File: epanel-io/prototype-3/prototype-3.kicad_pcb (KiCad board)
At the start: 2 copper layers, 87 x 68 mm, 32 parts, among them J1 Conn_01x07_Male, J2 Screw_Terminal_01x04, J3 Screw_Terminal_01x04, J4 Screw_Terminal_01x02, Q1 IRF830, Q2 IRF830, Q3 IRF830, U2 4N35, U3 4N35, U4 H11AA1, U5 H11AA1, U6 H11AA1

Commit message: wip proto 3
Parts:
- removed J4: Screw_Terminal_01x02, TerminalBlock:TerminalBlock_bornier-2_P5.08mm
- added C2: 2.2uF/63V, Capacitor_SMD:C_1206_3216Metric, F.Cu at (144.8, 69.8)
- added D4: 1N4007, Diode_SMD:D_SMA, F.Cu at (139.7, 67.3)
- added JP1: Jumper_2_Bridged, Connector_PinHeader_2.54mm:PinHeader_1x02_P2.54mm_Vertical, F.Cu at (95.2, 110.5)
- added Q4: IRF830, Package_TO_SOT_SMD:TO-263-3_TabPin2, F.Cu at (174.4, 73.7)
- added R16: 33KΩ/0.5W, Resistor_SMD:R_0805_2012Metric, F.Cu at (141.0, 61.0)
- added R17: 33KΩ/0.5W, Resistor_SMD:R_0805_2012Metric, F.Cu at (141.0, 72.4)
- added U1: Pico, MCU_RaspberryPi_and_Boards:RPi_Pico_SMD_TH, F.Cu at (149.9, 152.4)
- D1: value 4* 1N5408 -> 10V/0.4W; footprint Diode_SMD:Diode_Bridge_Diotec_SO-DIL-Slim -> Diode_SMD:D_SOD-123
- J1: value Conn_01x07_Male -> Conn_01x05_Male; footprint Connector_PinHeader_2.54mm:PinHeader_1x07_P2.54mm_Vertical -> Connector_PinHeader_2.54mm:PinHeader_1x05_P2.54mm_Vertical
- J2, J3: value Screw_Terminal_01x04 -> Screw_Terminal_01x03; footprint TerminalBlock:TerminalBlock_bornier-4_P5.08mm -> TerminalBlock:TerminalBlock_bornier-3_P5.08mm
- PS1: value HLK-PM12 -> HLK-PM01
- moved R3 109.8 mm to (215.5, 149.8)
- moved R5 105.9 mm to (215.5, 147.3)
- moved R4 98.3 mm to (212.1, 129.5)
- moved J3 86.9 mm to (111.8, 55.9), turned to -90 degrees
- moved R12 83.8 mm to (119.4, 55.9), turned to -90 degrees
- moved R13 76.2 mm to (119.4, 62.2), turned to -90 degrees
- moved U4 74.5 mm to (146.1, 127.0), turned to -90 degrees
- moved R1 58.5 mm to (168.9, 125.7), turned to 0 degrees
- moved R2 54.8 mm to (168.1, 123.2), turned to 0 degrees
- moved PS1 52.1 mm to (139.7, 17.8), turned to -90 degrees
- moved R14 50.2 mm to (124.5, 55.9), turned to -90 degrees
- moved D3 47.7 mm to (139.7, 55.9), turned to 90 degrees
- moved R15 47.6 mm to (124.5, 62.2), turned to -90 degrees
- moved U5 45.6 mm to (137.2, 127.0), turned to -90 degrees
- moved R10 45.2 mm to (121.9, 55.9), turned to -90 degrees
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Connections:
- D1 pad 1: Net-(D1-Pad1) -> Net-(C1-Pad1)
- D1 pad 2: Net-(D1-Pad2) -> Net-(C1-Pad2)
- D2 pad 1: Net-(C1-Pad1) -> Net-(C2-Pad1)
- D2 pad 2: Net-(C1-Pad2) -> Net-(C2-Pad2)
- D3 pad 2: Net-(D3-Pad2) -> NEUT
- J1 pad 1: +3V3 -> +5V
- J2 pad 1: Net-(D1-Pad3) -> LINE
- J2 pad 2: Net-(D1-Pad4) -> Net-(J2-Pad2)
- J3 pad 1: Net-(D3-Pad2) -> NEUT
- PS1 pad 1: Net-(D1-Pad3) -> LINE
- PS1 pad 2: Net-(J2-Pad4) -> NEUT
- PS1 pad 3: Net-(D1-Pad2) -> GND
- PS1 pad 4: Net-(PS1-Pad4) -> +5V
- Q1 pad 2: Net-(D1-Pad1) -> LINE
- Q1 pad 3: Net-(D1-Pad2) -> Net-(C1-Pad2)
- Q2 pad 1: Net-(Q2-Pad1) -> Net-(Q1-Pad1)
- Q2 pad 2: Net-(D3-Pad2) -> Net-(J2-Pad2)
- Q3 pad 1: Net-(Q2-Pad1) -> Net-(Q3-Pad1)
- Q3 pad 2: Net-(J3-Pad2) -> LINE
- Q3 pad 3: Net-(C1-Pad2) -> Net-(C2-Pad2)
- R1 pad 2: Net-(J1-Pad3) -> Net-(R1-Pad2)
- R10 pad 1: Net-(J3-Pad4) -> NEUT
- R11 pad 1: Net-(J3-Pad3) -> Net-(J3-Pad2)
- R12 pad 1: Net-(J4-Pad1) -> NEUT
- R12 pad 2: Net-(R12-Pad2) -> Net-(U5-Pad1)
- R13 pad 1: Net-(J4-Pad2) -> Net-(J3-Pad3)
- R14 pad 1: Net-(R14-Pad1) -> NEUT
- R14 pad 2: Net-(C1-Pad1) -> Net-(R14-Pad2)
- R15 pad 1: Net-(D3-Pad1) -> LINE
- R15 pad 2: Net-(R14-Pad1) -> Net-(R15-Pad2)
- R2 pad 2: Net-(J1-Pad5) -> Net-(R2-Pad2)
- R3 pad 1: Net-(J1-Pad4) -> Net-(R3-Pad1)
- R4 pad 1: Net-(J1-Pad6) -> Net-(R4-Pad1)
- R5 pad 1: Net-(J1-Pad7) -> Net-(R5-Pad1)
- R6 pad 2: Net-(D1-Pad2) -> Net-(C1-Pad2)
- R7 pad 1: Net-(Q2-Pad1) -> Net-(Q3-Pad1)
- R7 pad 2: Net-(C1-Pad2) -> Net-(C2-Pad2)
- R8 pad 1: Net-(J2-Pad4) -> Net-(R16-Pad2)
- R8 pad 2: Net-(R8-Pad2) -> Net-(C1-Pad1)
- R9 pad 1: Net-(J2-Pad3) -> Net-(R17-Pad2)
- R9 pad 2: Net-(R9-Pad2) -> Net-(C2-Pad1)
- U2 pad 5: Net-(PS1-Pad4) -> Net-(C1-Pad1)
- U3 pad 4: Net-(Q2-Pad1) -> Net-(Q3-Pad1)
- U3 pad 5: Net-(C1-Pad1) -> Net-(C2-Pad1)
- U4 pad 1: Net-(R8-Pad2) -> Net-(R10-Pad2)
- U4 pad 2: Net-(R9-Pad2) -> Net-(R11-Pad2)
- U4 pad 5: Net-(J1-Pad4) -> Net-(R3-Pad1)
- U5 pad 1: Net-(R10-Pad2) -> Net-(U5-Pad1)
- U5 pad 2: Net-(R11-Pad2) -> Net-(R13-Pad2)
- U5 pad 5: Net-(J1-Pad6) -> Net-(R4-Pad1)
- U6 pad 1: Net-(R12-Pad2) -> Net-(R14-Pad2)
- U6 pad 2: Net-(R13-Pad2) -> Net-(R15-Pad2)
- U6 pad 5: Net-(J1-Pad7) -> Net-(R5-Pad1)
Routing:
- net GND: track 122.8 -> 0.00 mm
- net LINE: track 0.00 -> 80.9 mm, vias 0 -> 2
- net Net-(J2-Pad4): track 64.1 -> 0.00 mm, vias 1 -> 0
- net Net-(Q3-Pad1): track 0.00 -> 59.0 mm, vias 0 -> 5
- net Net-(D1-Pad2): track 57.0 -> 0.00 mm
- net Net-(J1-Pad7): track 54.8 -> 0.00 mm
- net Net-(J2-Pad3): track 79.3 -> 25.4 mm, vias 1 -> 0
- net Net-(J1-Pad4): track 51.2 -> 0.00 mm, vias 2 -> 0
- net NEUT: track 0.00 -> 48.9 mm
- net Net-(J1-Pad6): track 45.8 -> 0.00 mm, vias 2 -> 0
- net Net-(J2-Pad2): track 0.00 -> 42.4 mm
- net Net-(D1-Pad3): track 41.7 -> 0.00 mm
- net Net-(D3-Pad2): track 39.7 -> 0.00 mm
- net Net-(R1-Pad1): track 37.9 -> 0.00 mm, vias 2 -> 0
- net Net-(PS1-Pad4): track 35.6 -> 0.00 mm
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
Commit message: wip proto 3
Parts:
- moved R16 158.6 mm to (70.7, 85.1)
- moved R17 158.6 mm to (70.7, 82.5)
- moved R15 149.4 mm to (71.1, 80.0)
- moved J3 93.4 mm to (188.0, 104.1)
- moved U6 77.8 mm to (90.2, 83.8), turned to 180 degrees
- moved U4 77.0 mm to (90.2, 66.0), turned to 180 degrees
- moved U5 76.4 mm to (90.2, 74.9), turned to 180 degrees
- moved U1 65.3 mm to (184.2, 96.5)
- moved U2 55.0 mm to (184.2, 86.4)
- moved U3 48.3 mm to (149.9, 104.1), turned to 90 degrees
- moved PS1 38.1 mm to (139.7, 55.9)
- moved R11 37.2 mm to (175.3, 86.7), turned to 90 degrees
- moved D3 36.8 mm to (170.2, 88.0), turned to 180 degrees
- moved D1 34.5 mm to (152.4, 88.0), turned to 180 degrees
- moved R14 33.2 mm to (177.8, 91.4), turned to -90 degrees
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- renumbered D3 to D1, D1 to D2, D4 to D3, D2 to D4, J3 to J1, J1 to J3, Q3 to Q2, Q2 to Q3, R12 to R1, R16 to R10, R17 to R11, R9 to R12, R1 to R13, R2 to R14, R4 to R15, R3 to R16, R5 to R17, R11 to R2, R10 to R3, R14 to R4, R13 to R5, R15 to R6, R6 to R7, R7 to R9, U2 to U1, U3 to U2, U1 to U3, U5 to U4, U4 to U5
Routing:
- net GND: track 0.00 -> 115.3 mm
- net +5V: track 0.00 -> 99.2 mm, vias 0 -> 2
- net Net-(J1-Pad3): track 0.00 -> 54.4 mm
- net Net-(J1-Pad4): track 0.00 -> 52.2 mm
- net Net-(J1-Pad5): track 0.00 -> 50.4 mm
- net Net-(Q1-Pad1): track 44.2 -> 87.5 mm, vias 3 -> 4
- net NEUT: track 48.9 -> 87.7 mm, vias 0 -> 2
- net Net-(C1-Pad1): track 13.9 -> 49.6 mm, vias 0 -> 2
- net Net-(JP1-Pad1): track 0.00 -> 22.7 mm
- net Net-(R1-Pad2): track 0.00 -> 20.0 mm
- net LINE: track 80.9 -> 68.3 mm, vias 2 -> 0
- net Net-(C2-Pad1): track 13.9 -> 26.3 mm, vias 0 -> 2
- net Net-(R2-Pad2): track 0.00 -> 9.76 mm
- net Net-(R2-Pad1): track 0.00 -> 8.59 mm
- net Net-(Q3-Pad1): track 59.0 -> 64.5 mm, vias 5 -> 4
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
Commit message: wip proto 3
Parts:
- moved R17 51.5 mm to (120.2, 96.5), turned to 180 degrees
- moved R16 49.5 mm to (120.2, 85.1), turned to 180 degrees
- moved R15 49.2 mm to (120.2, 82.5), turned to 180 degrees
- moved R4 42.6 mm to (111.8, 96.5), turned to 180 degrees
- moved U6 31.8 mm to (115.6, 102.9), turned to 0 degrees
- moved R3 29.7 mm to (111.8, 83.8), turned to 180 degrees
- moved U5 29.6 mm to (115.6, 90.2), turned to 0 degrees
- moved U4 27.9 mm to (115.6, 77.5), turned to 0 degrees
- moved R1 17.0 mm to (111.8, 71.1), turned to 180 degrees
- moved JP1 7.62 mm to (110.5, 113.0)
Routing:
- net Net-(R3-Pad1): track 0.00 -> 77.3 mm
- net Net-(R4-Pad1): track 0.00 -> 74.4 mm
- net Net-(R5-Pad1): track 0.00 -> 61.4 mm
- net GND: track 115.3 -> 166.4 mm, vias 0 -> 1
- net NEUT: track 87.7 -> 136.0 mm, vias 2 -> 5
- net Net-(R15-Pad2): track 0.00 -> 46.7 mm
- net +3V3: track 0.00 -> 36.6 mm, vias 0 -> 3
- net Net-(R11-Pad2): track 0.00 -> 32.9 mm
- net Net-(R13-Pad2): track 0.00 -> 19.2 mm
- net Net-(U5-Pad1): track 0.00 -> 3.83 mm
- net Net-(R14-Pad2): track 0.00 -> 3.83 mm
- net Net-(R10-Pad2): track 0.00 -> 3.83 mm
- net Net-(JP1-Pad1): track 22.7 -> 25.9 mm
- net +5V: track 99.2 -> 100.7 mm
- net Net-(C1-Pad1): track 49.6 -> 48.3 mm

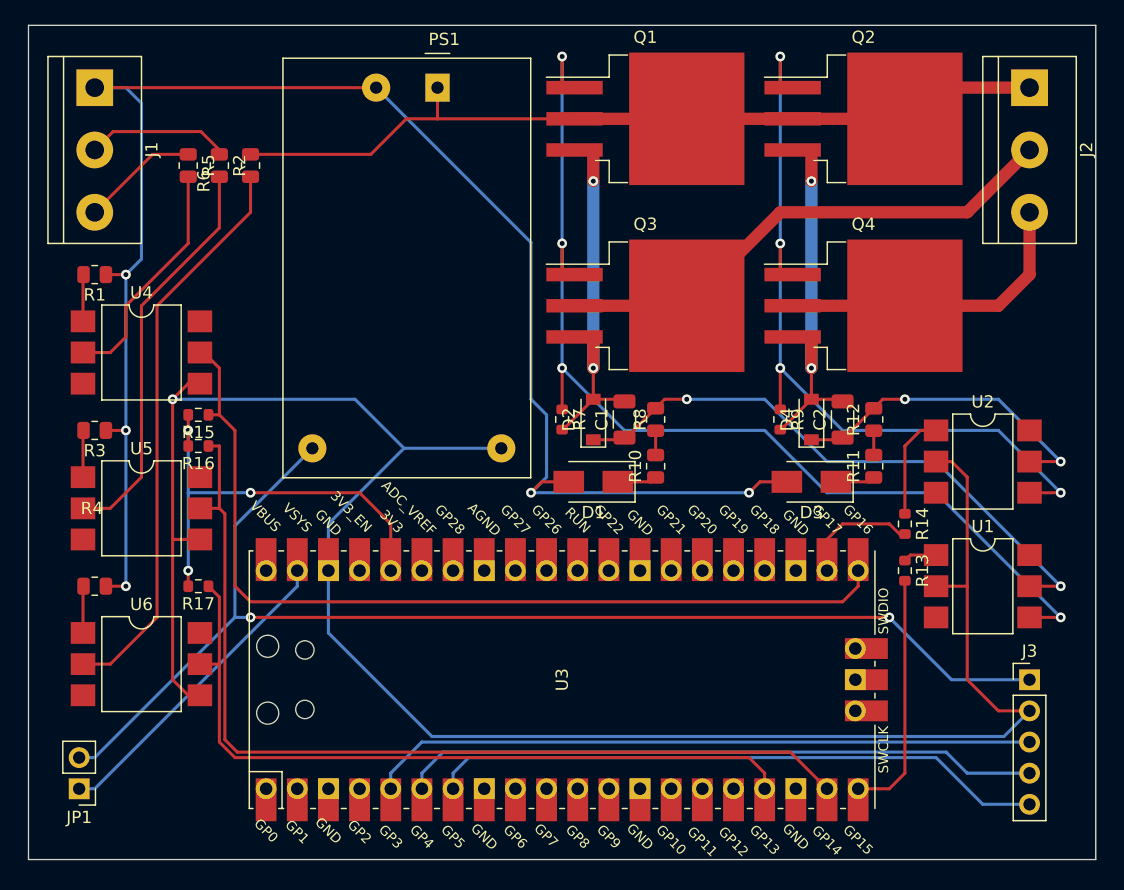
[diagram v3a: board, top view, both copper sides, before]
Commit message: fix annotations
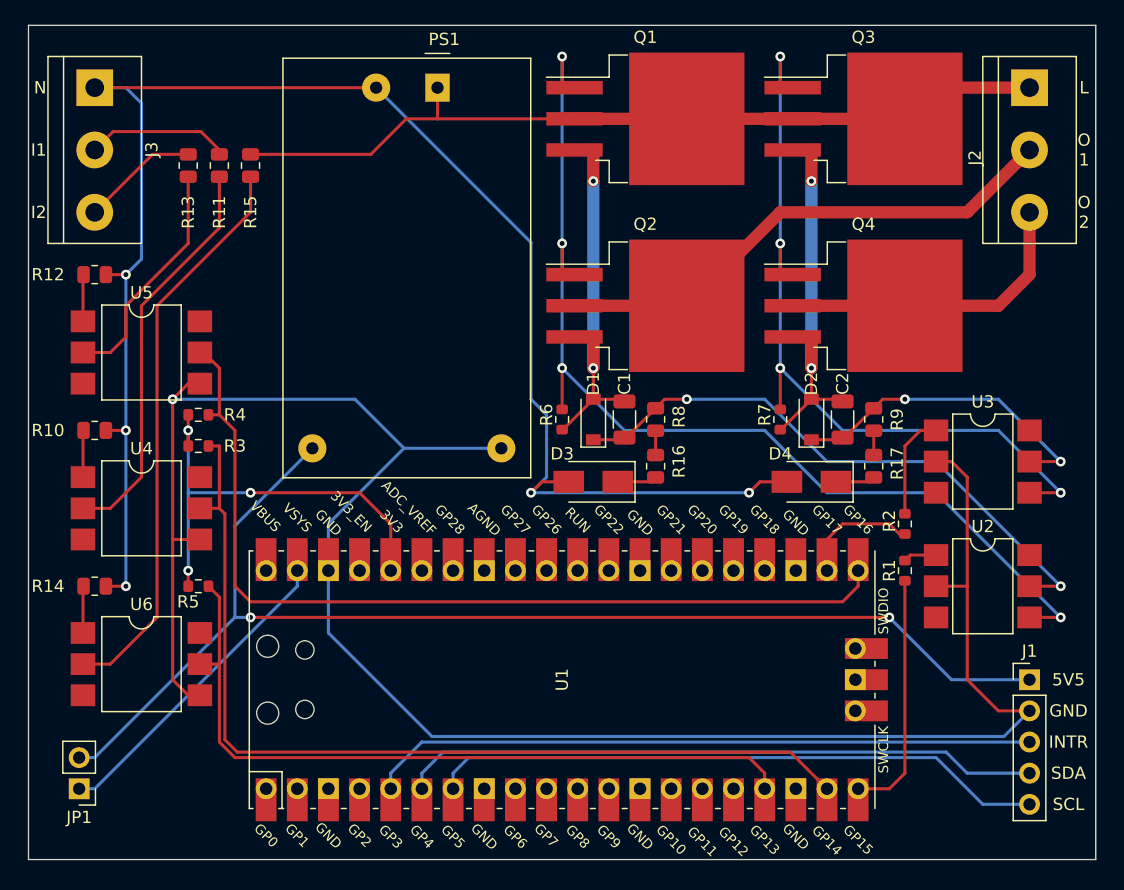
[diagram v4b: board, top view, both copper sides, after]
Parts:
- renumbered D2 to D1, D4 to D2, D1 to D3, D3 to D4, J3 to J1, J1 to J3, Q3 to Q2, Q2 to Q3, R13 to R1, R3 to R10, R2 to R11, R1 to R12, R5 to R13, R4 to R14, R6 to R15, R10 to R16, R11 to R17, R14 to R2, R16 to R3, R15 to R4, R17 to R5, R7 to R6, R9 to R7, R12 to R9, U3 to U1, U1 to U2, U2 to U3, U5 to U4, U4 to U5
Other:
- board text added: "5V5"
- board text added: "GND"
- board text added: "I1"
- board text added: "I2"
- board text added: "INTR"
- board text added: "L"
- board text added: "N"
- board text added: "O 1"
- board text added: "O 2"
- board text added: "SCL"
- board text added: "SDA"
